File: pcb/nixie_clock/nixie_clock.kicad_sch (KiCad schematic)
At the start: 0 parts

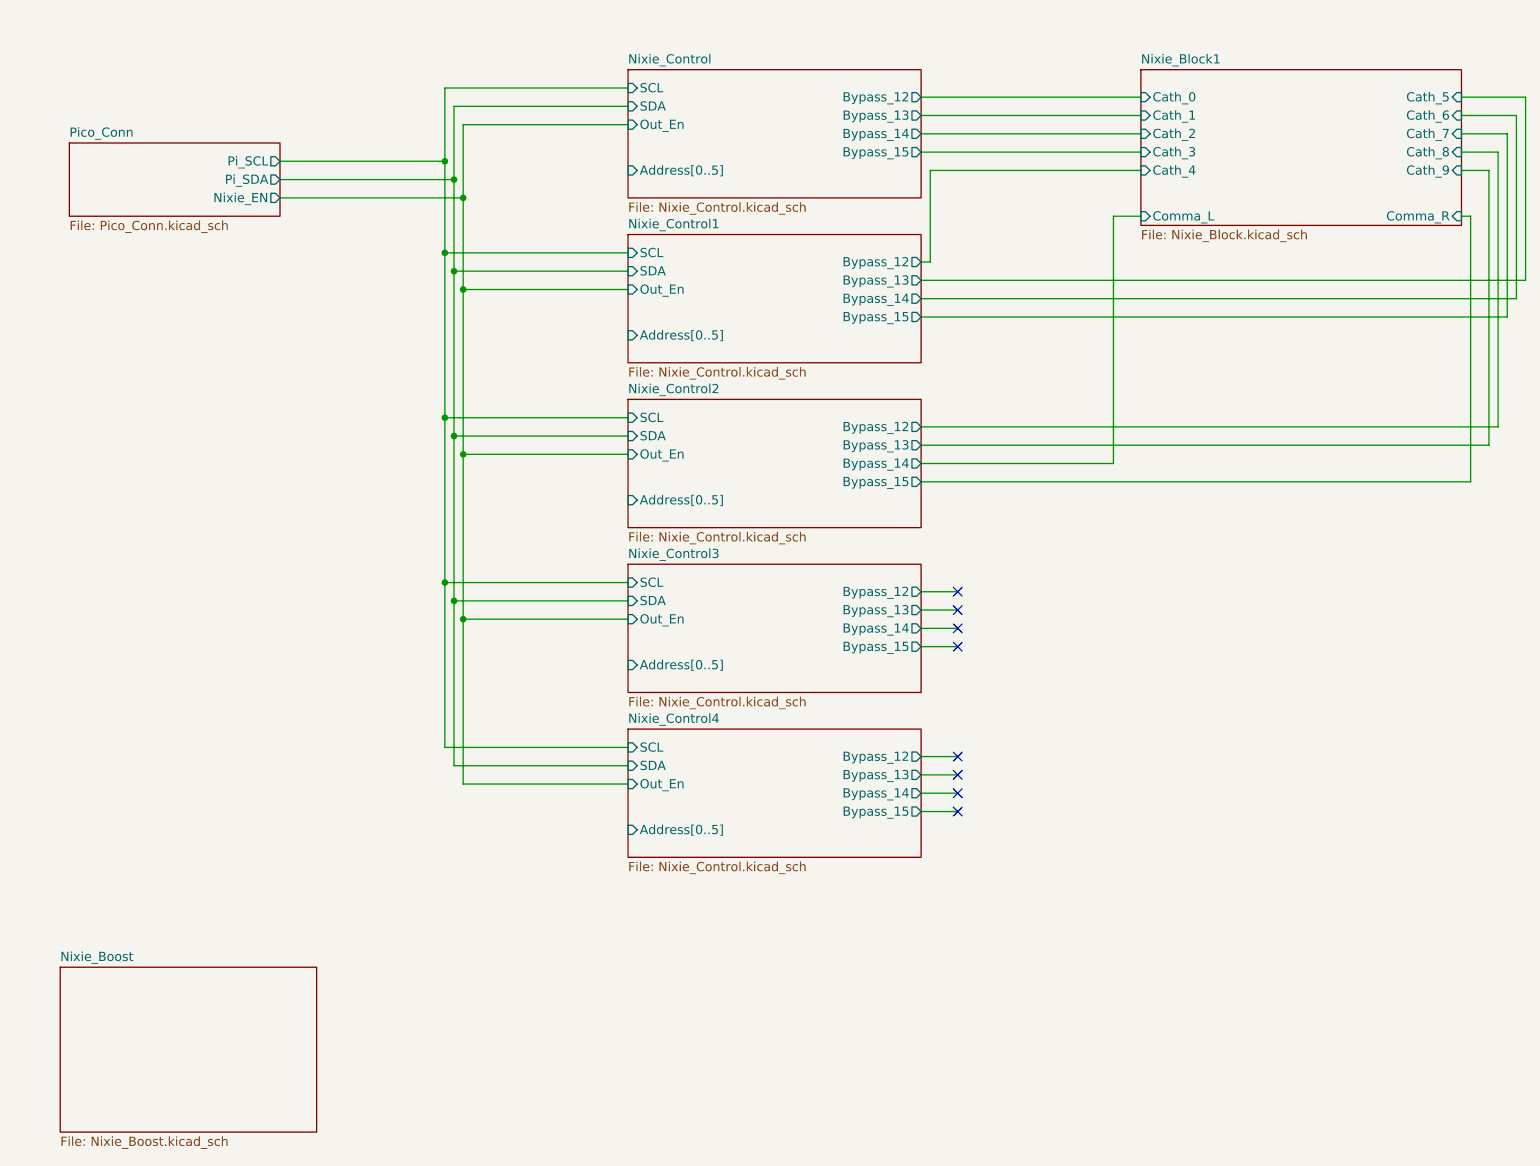
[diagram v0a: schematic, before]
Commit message: remove busses and output stuff
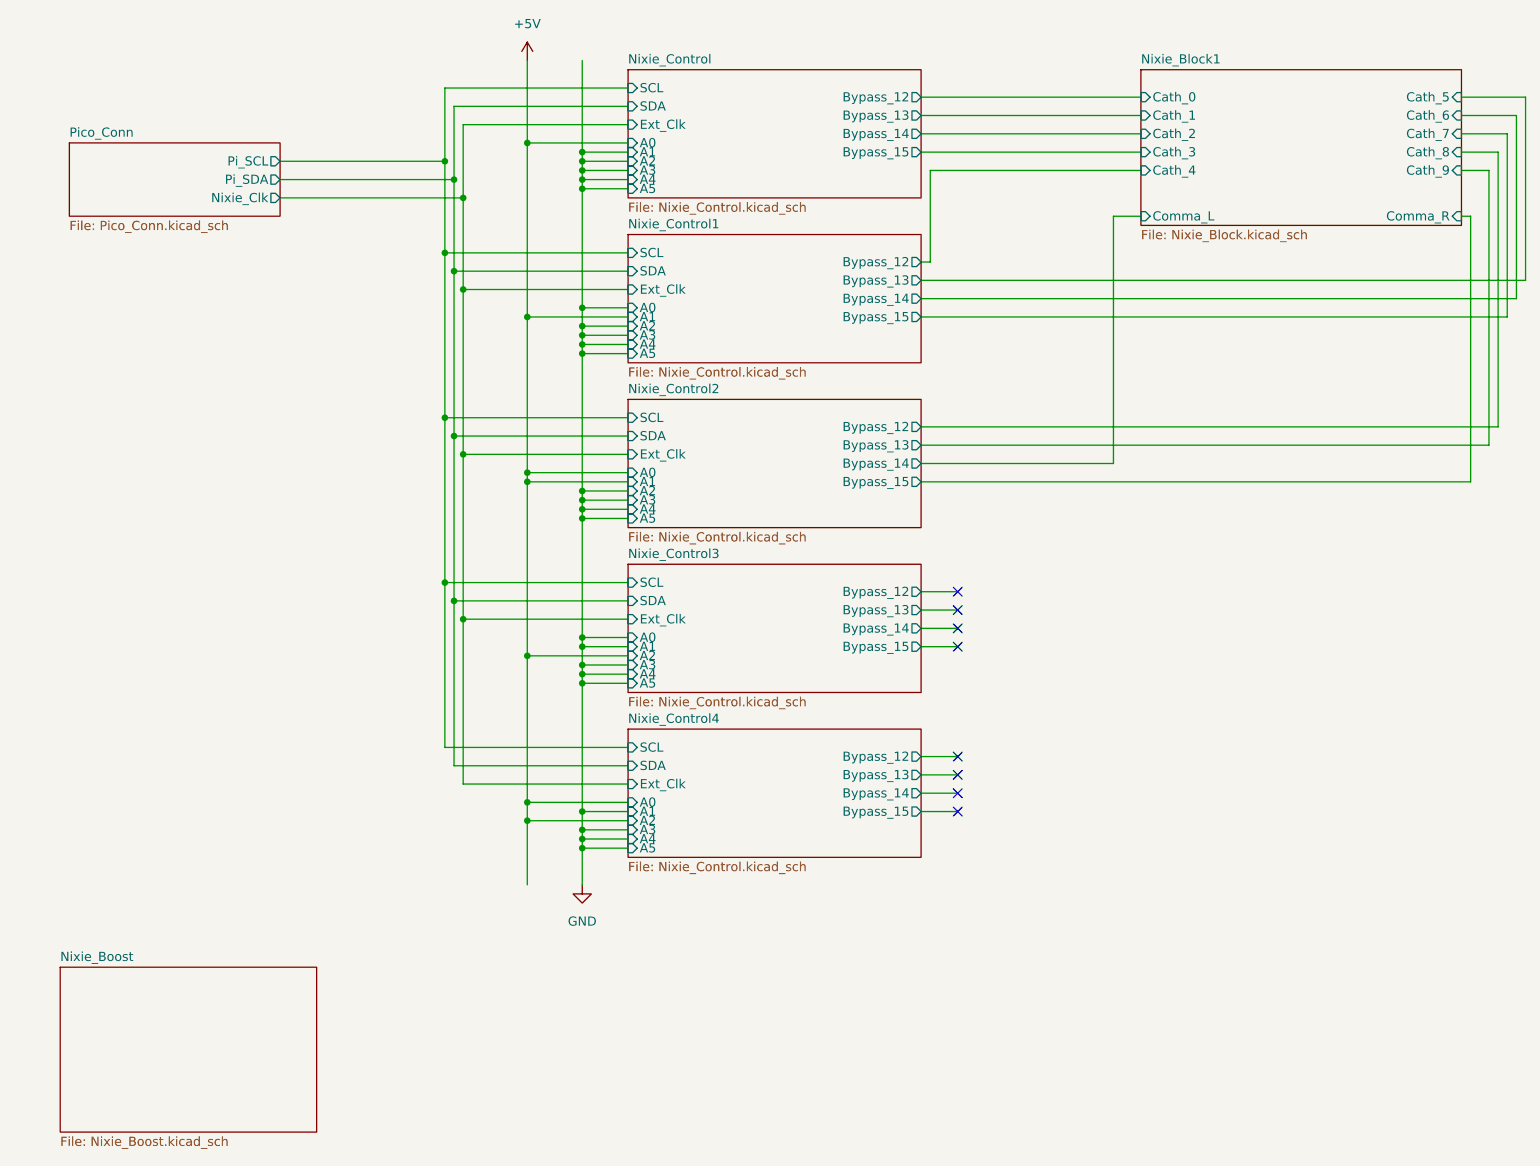
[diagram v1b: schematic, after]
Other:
- sheet Nixie_Control ports: added A0, A1, A2, A3, A4, A5, Ext_Clk; removed Address[0..5], Out_En
- sheet Nixie_Control1 ports: added A0, A1, A2, A3, A4, A5, Ext_Clk; removed Address[0..5], Out_En
- sheet Nixie_Control2 ports: added A0, A1, A2, A3, A4, A5, Ext_Clk; removed Address[0..5], Out_En
- sheet Nixie_Control3 ports: added A0, A1, A2, A3, A4, A5, Ext_Clk; removed Address[0..5], Out_En
- sheet Nixie_Control4 ports: added A0, A1, A2, A3, A4, A5, Ext_Clk; removed Address[0..5], Out_En
- sheet Pico_Conn ports: added Nixie_Clk; removed Nixie_EN

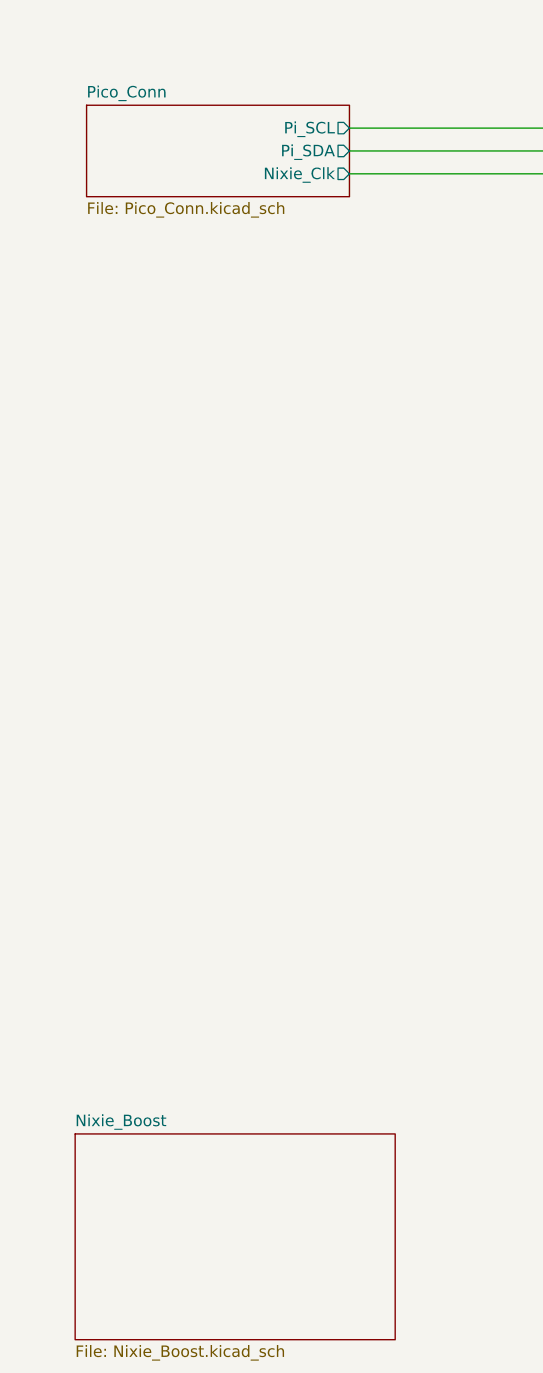
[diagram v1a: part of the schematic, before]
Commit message: schematic finalisation, footprint assignment and start on placeing components in layout.
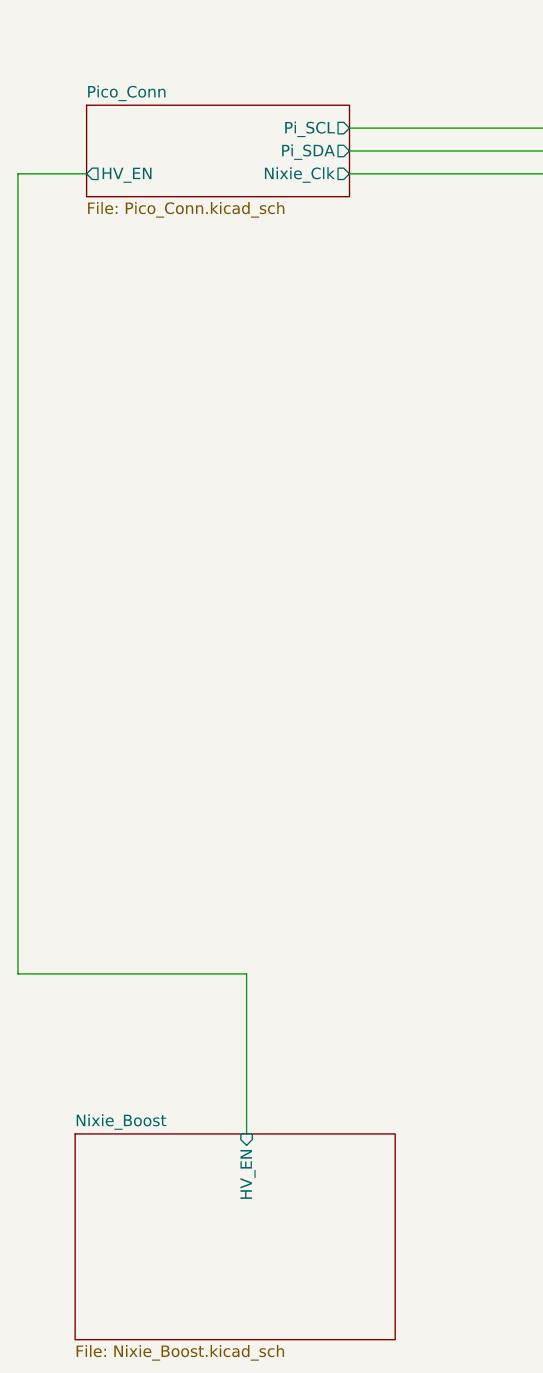
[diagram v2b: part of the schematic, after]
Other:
- sheet Nixie_Boost ports: added HV_EN; removed none
- sheet Pico_Conn ports: added HV_EN; removed none
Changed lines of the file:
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@@
+	(wire
+		(pts
+			(xy 29.21 133.35) (xy 54.61 133.35)
+		)
+		(stroke
+			(width 0)
+			(type default)
+		)
+	)
 	(wire
 		(pts
@@
 	(wire
 		(pts
+			(xy 29.21 44.45) (xy 29.21 133.35)
+		)
+		(stroke
+			(width 0)
+			(type default)
+		)
+	)
+	(wire
+		(pts
 			(xy 90.17 123.19) (xy 90.17 100.33)
 		)
@@
 	(wire
 		(pts
+			(xy 54.61 133.35) (xy 54.61 151.13)
+		)
+		(stroke
+			(width 0)
+			(type default)
+		)
+	)
+	(wire
+		(pts
 			(xy 100.33 107.95) (xy 100.33 128.27)
 		)
@@
 		(pts
 			(xy 114.3 125.73) (xy 91.44 125.73)
+		)
+		(stroke
+			(width 0)
+			(type default)
+		)
+	)
+	(wire
+		(pts
+			(xy 36.83 44.45) (xy 29.21 44.45)
 		)
 		(stroke
@@
 			)
 		)
+		(pin "HV_EN" output
+			(at 36.83 44.45 180)
+			(effects
+				(font
+					(size 1.27 1.27)
+				)
+				(justify left)
+			)
+		)
 		(instances
 			(project "nixie_clock"
@@
 			)
 		)
+		(pin "HV_EN" input
+			(at 54.61 151.13 90)
+			(effects
+				(font
+					(size 1.27 1.27)
+				)
+				(justify right)
+			)
+		)

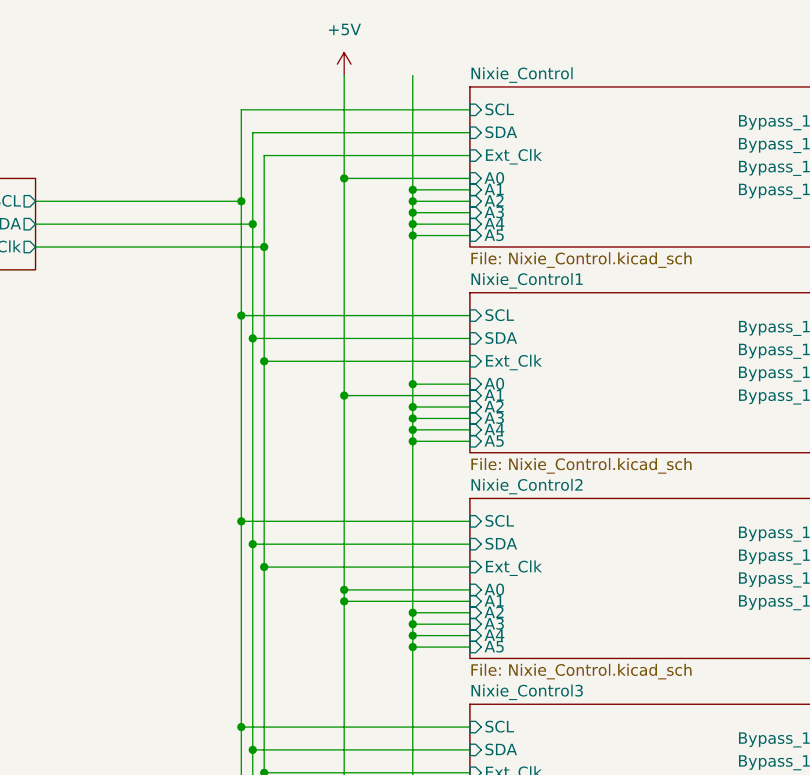
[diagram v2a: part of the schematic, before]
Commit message: hierarkical pcb switch and finishing of layout time for final checks need to redo nixie tube layout
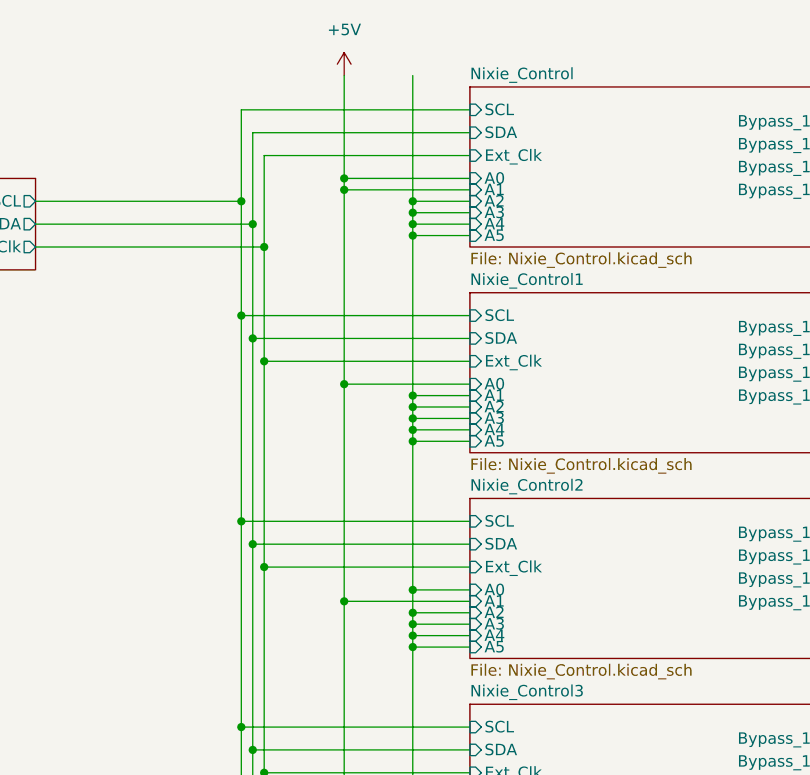
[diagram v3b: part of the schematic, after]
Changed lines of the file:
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@@
+	)
+	(junction
+		(at 100.33 38.1)
+		(diameter 0)
+		(color 0 0 0 0)
 	)
 	(junction
@@
 	)
 	(junction
-		(at 100.33 60.96)
-		(diameter 0)
-		(color 0 0 0 0)
-	)
-	(junction
-		(at 107.95 38.1)
-		(diameter 0)
-		(color 0 0 0 0)
-	)
-	(junction
 		(at 107.95 39.37)
 		(diameter 0)
@@
 	)
 	(junction
+		(at 107.95 60.96)
+		(diameter 0)
+		(color 0 0 0 0)
+	)
+	(junction
 		(at 100.33 107.95)
 		(diameter 0)
@@
 	)
 	(junction
+		(at 107.95 82.55)
+		(diameter 0)
+		(color 0 0 0 0)
+	)
+	(junction
 		(at 88.9 52.07)
 		(diameter 0)
@@
 	)
 	(junction
+		(at 100.33 59.69)
+		(diameter 0)
+		(color 0 0 0 0)
+	)
+	(junction
 		(at 107.95 109.22)
 		(diameter 0)
@@
 	)
 	(junction
-		(at 100.33 82.55)
-		(diameter 0)
-		(color 0 0 0 0)
-	)
-	(junction
 		(at 107.95 111.76)
 		(diameter 0)
@@
 	(junction
 		(at 107.95 66.04)
-		(diameter 0)
-		(color 0 0 0 0)
-	)
-	(junction
-		(at 107.95 59.69)
 		(diameter 0)
 		(color 0 0 0 0)
@@
 	(wire
 		(pts
-			(xy 100.33 60.96) (xy 114.3 60.96)
-		)
-		(stroke
-			(width 0)
-			(type default)
-		)
-	)
-	(wire
-		(pts
 			(xy 90.17 41.91) (xy 90.17 54.61)
 		)
@@
 	(wire
 		(pts
-			(xy 100.33 60.96) (xy 100.33 82.55)
+			(xy 100.33 36.83) (xy 100.33 38.1)
 		)
 		(stroke
@@
 	(wire
 		(pts
+			(xy 107.95 82.55) (xy 107.95 85.09)
+		)
+		(stroke
+			(width 0)
+			(type default)
+		)
+	)
+	(wire
+		(pts
 			(xy 107.95 63.5) (xy 107.95 64.77)
 		)
@@
 	(wire
 		(pts
+			(xy 107.95 82.55) (xy 114.3 82.55)
+		)
+		(stroke
+			(width 0)
+			(type default)
+		)
+	)
+	(wire
+		(pts
 			(xy 107.95 63.5) (xy 114.3 63.5)
 		)
@@
 	(wire
 		(pts
+			(xy 107.95 60.96) (xy 114.3 60.96)
+		)
+		(stroke
+			(width 0)
+			(type default)
+		)
+	)
+	(wire
+		(pts
 			(xy 154.94 83.82) (xy 231.14 83.82)
 		)
@@
 	(wire
 		(pts
-			(xy 107.95 59.69) (xy 114.3 59.69)
-		)
-		(stroke
-			(width 0)
-			(type default)
-		)
-	)
-	(wire
-		(pts
 			(xy 107.95 110.49) (xy 114.3 110.49)
 		)
@@
 	(wire
 		(pts
-			(xy 107.95 66.04) (xy 107.95 85.09)
+			(xy 107.95 66.04) (xy 107.95 82.55)
 		)
 		(stroke
@@
 	(wire
 		(pts
-			(xy 100.33 36.83) (xy 100.33 60.96)
-		)
-		(stroke
-			(width 0)
-			(type default)
-		)
-	)
-	(wire
-		(pts
 			(xy 234.95 76.2) (xy 154.94 76.2)
 		)
@@
 	(wire
 		(pts
+			(xy 100.33 38.1) (xy 114.3 38.1)
+		)
+		(stroke
+			(width 0)
+			(type default)
+		)
+	)
+	(wire
+		(pts
 			(xy 154.94 78.74) (xy 233.68 78.74)
 		)
@@
 	(wire
 		(pts
-			(xy 107.95 38.1) (xy 107.95 39.37)
-		)
-		(stroke
-			(width 0)
-			(type default)
-		)
-	)
-	(wire
-		(pts
-			(xy 107.95 25.4) (xy 107.95 38.1)
+			(xy 107.95 25.4) (xy 107.95 39.37)
 		)
 		(stroke
@@
 	(wire
 		(pts
-			(xy 100.33 82.55) (xy 114.3 82.55)
-		)
-		(stroke
-			(width 0)
-			(type default)
-		)
-	)
-	(wire
-		(pts
-			(xy 107.95 59.69) (xy 107.95 62.23)
+			(xy 107.95 43.18) (xy 107.95 60.96)
 		)
 		(stroke
@@
 	(wire
 		(pts
-			(xy 107.95 43.18) (xy 107.95 59.69)
-		)
-		(stroke
-			(width 0)
-			(type default)
-		)
-	)
-	(wire
-		(pts
 			(xy 107.95 43.18) (xy 114.3 43.18)
 		)
@@
 	(wire
 		(pts
+			(xy 100.33 59.69) (xy 114.3 59.69)
+		)
+		(stroke
+			(width 0)
+			(type default)
+		)
+	)
+	(wire
+		(pts
 			(xy 100.33 128.27) (xy 114.3 128.27)
 		)
@@
 	(wire
 		(pts
-			(xy 100.33 82.55) (xy 100.33 83.82)
+			(xy 100.33 38.1) (xy 100.33 59.69)
 		)
 		(stroke
@@
 	(wire
 		(pts
-			(xy 107.95 38.1) (xy 114.3 38.1)
-		)
-		(stroke
-			(width 0)
-			(type default)
-		)
-	)
-	(wire
-		(pts
 			(xy 91.44 34.29) (xy 91.44 44.45)
 		)
@@
 	(wire
 		(pts
+			(xy 100.33 59.69) (xy 100.33 83.82)
+		)
+		(stroke
+			(width 0)
+			(type default)
+		)
+	)
+	(wire
+		(pts
 			(xy 88.9 29.21) (xy 88.9 39.37)
 		)
@@
 		)
 		(stroke
+			(width 0)
+			(type default)
+		)
+	)
+	(wire
+		(pts
+			(xy 107.95 60.96) (xy 107.95 62.23)
+		)
+		(stroke

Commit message: added grounding
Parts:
- added J1: Conn_01x06_Pin, Connector_Molex:Molex_KK-254_AE-6410-06A_1x06_P2.54mm_Vertical, symbol Connector:Conn_01x06_Pin
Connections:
- net GND: now also J1.1 (Pin_1), J1.2 (Pin_2), J1.3 (Pin_3), J1.4 (Pin_4), J1.5 (Pin_5), J1.6 (Pin_6)
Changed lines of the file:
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@@
+	)
+	(junction
+		(at 124.46 162.56)
+		(diameter 0)
+		(color 0 0 0 0)
 	)
 	(junction
@@
 	)
 	(junction
+		(at 121.92 162.56)
+		(diameter 0)
+		(color 0 0 0 0)
+	)
+	(junction
 		(at 88.9 39.37)
 		(diameter 0)
@@
 	)
 	(junction
+		(at 129.54 162.56)
+		(diameter 0)
+		(color 0 0 0 0)
+	)
+	(junction
 		(at 107.95 60.96)
 		(diameter 0)
@@
 	(junction
 		(at 107.95 106.68)
+		(diameter 0)
+		(color 0 0 0 0)
+	)
+	(junction
+		(at 127 162.56)
 		(diameter 0)
 		(color 0 0 0 0)
@@
 	(wire
 		(pts
+			(xy 127 162.56) (xy 127 166.37)
+		)
+		(stroke
+			(width 0)
+			(type default)
+		)
+	)
+	(wire
+		(pts
 			(xy 29.21 44.45) (xy 29.21 133.35)
 		)
@@
 	(wire
 		(pts
+			(xy 119.38 162.56) (xy 121.92 162.56)
+		)
+		(stroke
+			(width 0)
+			(type default)
+		)
+	)
+	(wire
+		(pts
 			(xy 234.95 76.2) (xy 154.94 76.2)
 		)
@@
 	(wire
 		(pts
+			(xy 124.46 162.56) (xy 127 162.56)
+		)
+		(stroke
+			(width 0)
+			(type default)
+		)
+	)
+	(wire
+		(pts
 			(xy 90.17 54.61) (xy 90.17 77.47)
 		)
@@
 	(wire
 		(pts
+			(xy 129.54 162.56) (xy 132.08 162.56)
+		)
+		(stroke
+			(width 0)
+			(type default)
+		)
+	)
+	(wire
+		(pts
 			(xy 107.95 43.18) (xy 107.95 60.96)
 		)
@@
 	(wire
 		(pts
+			(xy 121.92 162.56) (xy 124.46 162.56)
+		)
+		(stroke
+			(width 0)
+			(type default)
+		)
+	)
+	(wire
+		(pts
 			(xy 107.95 133.35) (xy 107.95 134.62)
 		)
@@
 	(wire
 		(pts
+			(xy 127 162.56) (xy 129.54 162.56)
+		)
+		(stroke
+			(width 0)
+			(type default)
+		)
+	)
+	(wire
+		(pts
 			(xy 229.87 38.1) (xy 234.95 38.1)
 		)
@@
 		)
 	)
+	(symbol
+		(lib_id "power:GND")
+		(at 127 166.37 0)
+		(unit 1)
+		(exclude_from_sim no)
+		(in_bom yes)
+		(on_board yes)
+		(dnp no)
+		(fields_autoplaced yes)
+		(property "Reference" "#PWR0106"
+			(at 127 172.72 0)
+			(effects
+				(font
+					(size 1.27 1.27)
+				)
+				(hide yes)
+			)
+		)
+		(property "Value" "GND"
+			(at 127 171.45 0)
+			(effects
+				(font
+					(size 1.27 1.27)
+				)
+			)
+		)
+		(property "Footprint" ""
+			(at 127 166.37 0)
+			(effects
+				(font
+					(size 1.27 1.27)
+				)
+				(hide yes)
+			)
+		)
+		(property "Datasheet" ""
+			(at 127 166.37 0)
+			(effects
+				(font
+					(size 1.27 1.27)
+				)
+				(hide yes)
+			)
+		)
+		(property "Description" "Power symbol creates a global label with name \"GND\" , ground"
+			(at 127 166.37 0)
+			(effects
+				(font
+					(size 1.27 1.27)
+				)
+				(hide yes)
+			)
+		)
+		(pin "1"
+		)
+		(instances
+			(project ""
+				(path "/87768a79-2a56-4b5f-a764-e1a4021de947"
+					(reference "#PWR0106")
+					(unit 1)
+				)
+			)
+		)
+	)
+	(symbol
+		(lib_id "Connector:Conn_01x06_Pin")
+		(at 127 157.48 270)
+		(unit 1)
+		(exclude_from_sim no)
+		(in_bom yes)
+		(on_board yes)
+		(dnp yes)
+		(fields_autoplaced yes)
+		(property "Reference" "J1"
+			(at 125.73 152.4 90)
+			(effects
+				(font
+					(size 1.27 1.27)
+				)
+			)
+		)
+		(property "Value" "Conn_01x06_Pin"
+			(at 125.73 154.94 90)
+			(effects
+				(font
+					(size 1.27 1.27)
+				)
+			)
+		)
+		(property "Footprint" "Connector_Molex:Molex_KK-254_AE-6410-06A_1x06_P2.54mm_Vertical"
+			(at 127 157.48 0)
+			(effects
+				(font
+					(size 1.27 1.27)
+				)
+				(hide yes)
+			)
+		)
+		(property "Datasheet" "~"
+			(at 127 157.48 0)
+			(effects
+				(font
+					(size 1.27 1.27)
+				)
+				(hide yes)
+			)
+		)
+		(property "Description" "Generic connector, single row, 01x06, script generated"
+			(at 127 157.48 0)
+			(effects
+				(font
+					(size 1.27 1.27)
+				)
+				(hide yes)
+			)
+		)
+		(pin "1"
+		)
+		(pin "2"
+		)
+		(pin "3"
+		)
+		(pin "5"
+		)
+		(pin "4"
+		)
+		(pin "6"
+		)
+		(instances
+			(project ""
+				(path "/87768a79-2a56-4b5f-a764-e1a4021de947"
+					(reference "J1")
+					(unit 1)
+				)
+			)
+		)
+	)
